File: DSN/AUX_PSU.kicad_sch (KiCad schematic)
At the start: 9 parts

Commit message: Added Footprints
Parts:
- U?: footprint (none) -> Package_TO_SOT_SMD:SOT-563; MFR PN (none) -> TPS62A02ADRLR
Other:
- title: (none) -> 3V3 Aux PSU
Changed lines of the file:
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@@
 (kicad_sch (version 20211123) (generator eeschema)
   (paper "A4")
+  (title_block
+    (title "3V3 Aux PSU")
+    (date "2023-03-07")
+    (rev "A")
+    (comment 1 "Designed by DragonEnjouer :3")
+  )
   (junction (at 185.42 88.9) (diameter 0) (color 0 0 0 0)
   )
@@
     (property "Reference" "U?" (id 0) (at 128.27 81.28 0))
     (property "Value" "TPS62A02A" (id 1) (at 128.27 83.82 0))
-    (property "Footprint" "" (id 2) (at 144.78 92.71 0)
-      (effects (font (size 1.27 1.27)) hide)
-    )
-    (property "Datasheet" "" (id 3) (at 144.78 92.71 0)
-      (effects (font (size 1.27 1.27)) hide)
-    )
+    (property "Footprint" "Package_TO_SOT_SMD:SOT-563" (id 2) (at 144.78 92.71 0)
+      (effects (font (size 1.27 1.27)) hide)
+    )
+    (property "Datasheet" "https://www.ti.com/lit/ds/symlink/tps62a02a.pdf" (id 3) (at 144.78 92.71 0)
+      (effects (font (size 1.27 1.27)) hide)
+    )
+    (property "MFR PN" "TPS62A02ADRLR" (id 4) (at 119.38 101.6 0)
+      (effects (font (size 1.27 1.27)) hide)
+    )

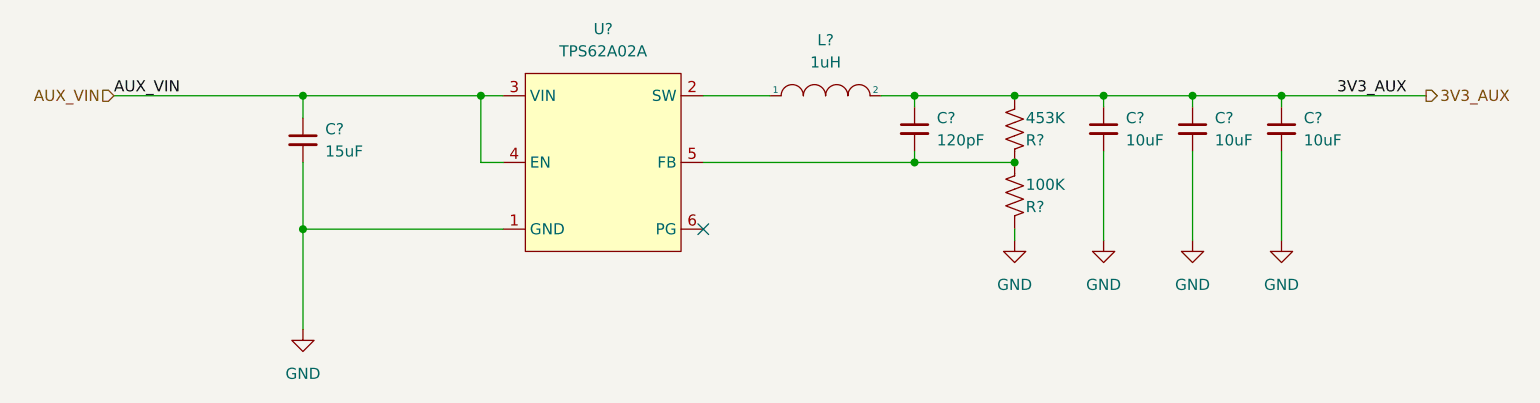
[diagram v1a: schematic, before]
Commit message: Added component ref des
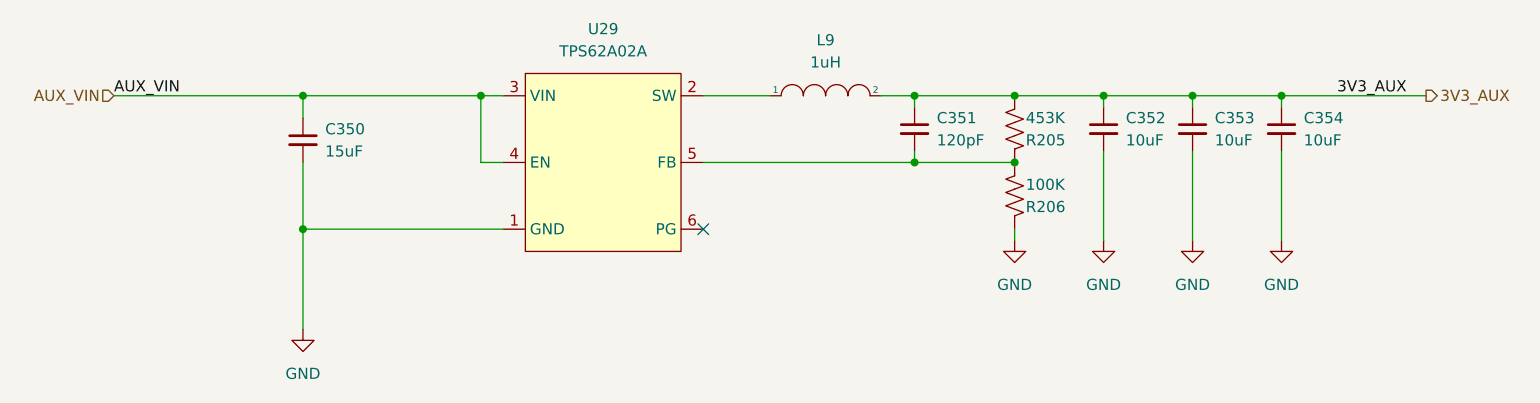
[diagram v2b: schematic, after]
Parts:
- gave numbers to parts that had none: 9
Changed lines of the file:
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@@
   (symbol (lib_id "Device:C_Small") (at 185.42 92.71 0) (unit 1)
     (in_bom yes) (on_board yes) (fields_autoplaced)
-    (property "Reference" "C?" (id 0) (at 187.96 91.4462 0)
+    (property "Reference" "C352" (id 0) (at 187.96 91.4462 0)
       (effects (font (size 1.27 1.27)) (justify left))
     )
@@
   (symbol (lib_id "power:GND") (at 175.26 105.41 0) (unit 1)
     (in_bom yes) (on_board yes) (fields_autoplaced)
-    (property "Reference" "#PWR?" (id 0) (at 175.26 111.76 0)
+    (property "Reference" "#PWR0579" (id 0) (at 175.26 111.76 0)
       (effects (font (size 1.27 1.27)) hide)
     )
@@
   (symbol (lib_id "pspice:INDUCTOR") (at 153.67 88.9 0) (unit 1)
     (in_bom yes) (on_board yes) (fields_autoplaced)
-    (property "Reference" "L?" (id 0) (at 153.67 82.55 0))
+    (property "Reference" "L9" (id 0) (at 153.67 82.55 0))
     (property "Value" "1uH" (id 1) (at 153.67 85.09 0))
     (property "Footprint" "Inductor_SMD:L_1008_2520Metric" (id 2) (at 153.67 88.9 0)
@@
   (symbol (lib_id "power:GND") (at 93.98 115.57 0) (unit 1)
     (in_bom yes) (on_board yes) (fields_autoplaced)
-    (property "Reference" "#PWR?" (id 0) (at 93.98 121.92 0)
+    (property "Reference" "#PWR0578" (id 0) (at 93.98 121.92 0)
       (effects (font (size 1.27 1.27)) hide)
     )
@@
   (symbol (lib_id "Device:C_Small") (at 93.98 93.98 0) (unit 1)
     (in_bom yes) (on_board yes) (fields_autoplaced)
-    (property "Reference" "C?" (id 0) (at 96.52 92.7162 0)
+    (property "Reference" "C350" (id 0) (at 96.52 92.7162 0)
       (effects (font (size 1.27 1.27)) (justify left))
     )
@@
   (symbol (lib_id "Device:C_Small") (at 163.83 92.71 0) (unit 1)
     (in_bom yes) (on_board yes) (fields_autoplaced)
-    (property "Reference" "C?" (id 0) (at 166.37 91.4462 0)
+    (property "Reference" "C351" (id 0) (at 166.37 91.4462 0)
       (effects (font (size 1.27 1.27)) (justify left))
     )
@@
   (symbol (lib_id "Device:C_Small") (at 195.58 92.71 0) (unit 1)
     (in_bom yes) (on_board yes) (fields_autoplaced)
-    (property "Reference" "C?" (id 0) (at 198.12 91.4462 0)
+    (property "Reference" "C353" (id 0) (at 198.12 91.4462 0)
       (effects (font (size 1.27 1.27)) (justify left))
     )
@@
   (symbol (lib_id "Device:C_Small") (at 205.74 92.71 0) (unit 1)
     (in_bom yes) (on_board yes) (fields_autoplaced)
-    (property "Reference" "C?" (id 0) (at 208.28 91.4462 0)
+    (property "Reference" "C354" (id 0) (at 208.28 91.4462 0)
       (effects (font (size 1.27 1.27)) (justify left))
     )
@@
   (symbol (lib_id "Device:R_US") (at 175.26 92.71 0) (mirror y) (unit 1)
     (in_bom yes) (on_board yes)
-    (property "Reference" "R?" (id 0) (at 176.53 93.98 0)
+    (property "Reference" "R205" (id 0) (at 176.53 93.98 0)
       (effects (font (size 1.27 1.27)) (justify right))
     )
@@
   (symbol (lib_id "power:GND") (at 205.74 105.41 0) (unit 1)
     (in_bom yes) (on_board yes) (fields_autoplaced)
-    (property "Reference" "#PWR?" (id 0) (at 205.74 111.76 0)
+    (property "Reference" "#PWR0582" (id 0) (at 205.74 111.76 0)
       (effects (font (size 1.27 1.27)) hide)
     )
@@
   (symbol (lib_id "Device:R_US") (at 175.26 100.33 0) (mirror y) (unit 1)
     (in_bom yes) (on_board yes)
-    (property "Reference" "R?" (id 0) (at 176.53 101.6 0)
+    (property "Reference" "R206" (id 0) (at 176.53 101.6 0)
       (effects (font (size 1.27 1.27)) (justify right))
     )
@@
   (symbol (lib_id "Regulator_Switching:TPS62A02A") (at 119.38 101.6 0) (unit 1)
     (in_bom yes) (on_board yes) (fields_autoplaced)
-    (property "Reference" "U?" (id 0) (at 128.27 81.28 0))
+    (property "Reference" "U29" (id 0) (at 128.27 81.28 0))
     (property "Value" "TPS62A02A" (id 1) (at 128.27 83.82 0))
     (property "Footprint" "Package_TO_SOT_SMD:SOT-563" (id 2) (at 144.78 92.71 0)
@@
   (symbol (lib_id "power:GND") (at 185.42 105.41 0) (unit 1)
     (in_bom yes) (on_board yes) (fields_autoplaced)
-    (property "Reference" "#PWR?" (id 0) (at 185.42 111.76 0)
+    (property "Reference" "#PWR0580" (id 0) (at 185.42 111.76 0)
       (effects (font (size 1.27 1.27)) hide)
     )
@@
   (symbol (lib_id "power:GND") (at 195.58 105.41 0) (unit 1)
     (in_bom yes) (on_board yes) (fields_autoplaced)
-    (property "Reference" "#PWR?" (id 0) (at 195.58 111.76 0)
-      (effects (font (size 1.27 1.27)) hide)
-    )
+    (property "Reference" "#PWR0581" (id 0) (at 195.58 111.76 0)
+      (effects (font (size 1.27 1.27)) hide)
+    )

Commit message: Fixed all ERC Errors
Warnings can be ignored
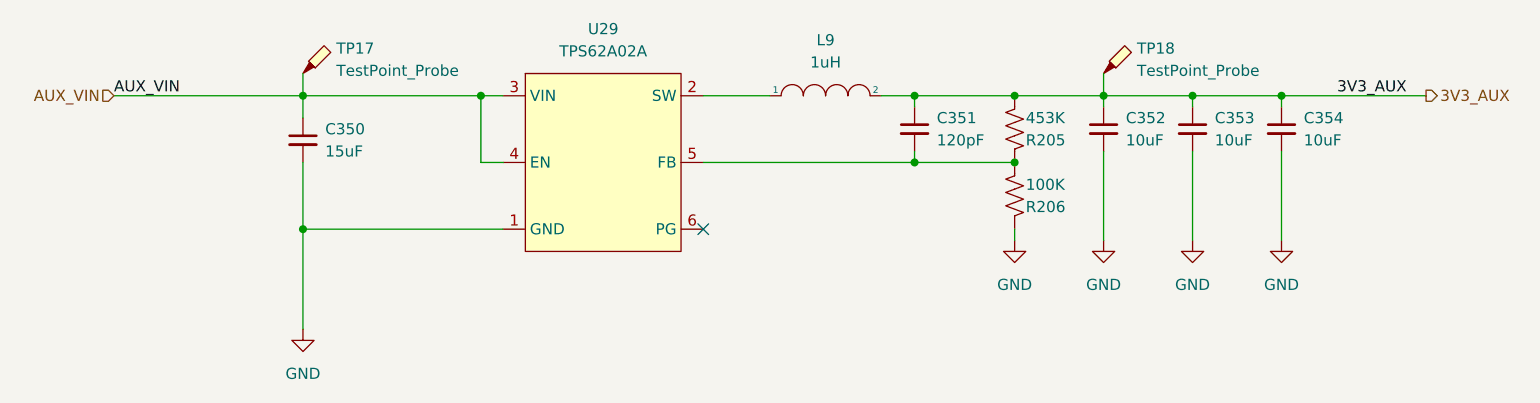
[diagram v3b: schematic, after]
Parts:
- added TP17, TP18: TestPoint_Probe, TestPoint:TestPoint_Loop_D2.50mm_Drill1.85mm, symbol Connector:TestPoint_Probe
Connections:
- net 3V3_AUX: now also TP18.1
- net AUX_VIN: now also TP17.1
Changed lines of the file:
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@@
+    (stroke (width 0) (type default) (color 0 0 0 0))
+  )
+  (wire (pts (xy 93.98 86.36) (xy 93.98 88.9))
     (stroke (width 0) (type default) (color 0 0 0 0))
   )
@@
   )
   (wire (pts (xy 185.42 95.25) (xy 185.42 105.41))
+    (stroke (width 0) (type default) (color 0 0 0 0))
+  )
+  (wire (pts (xy 185.42 86.36) (xy 185.42 88.9))
     (stroke (width 0) (type default) (color 0 0 0 0))
   )
@@
     (pin "1")
     (pin "2")
+  )
+  (symbol (lib_id "Connector:TestPoint_Probe") (at 185.42 86.36 0) (unit 1)
+    (in_bom yes) (on_board yes)
+    (property "Reference" "TP18" (id 0) (at 189.23 83.5024 0)
+      (effects (font (size 1.27 1.27)) (justify left))
+    )
+    (property "Value" "TestPoint_Probe" (id 1) (at 189.23 86.0424 0)
+      (effects (font (size 1.27 1.27)) (justify left))
+    )
+    (property "Footprint" "TestPoint:TestPoint_Loop_D2.50mm_Drill1.85mm" (id 2) (at 190.5 86.36 0)
+      (effects (font (size 1.27 1.27)) hide)
+    )
+    (property "Datasheet" "~" (id 3) (at 190.5 86.36 0)
+      (effects (font (size 1.27 1.27)) hide)
+    )
+    (pin "1")
   )
   (symbol (lib_id "power:GND") (at 93.98 115.57 0) (unit 1)
@@
       (effects (font (size 1.27 1.27)) hide)
     )
+    (pin "1")
+  )
+  (symbol (lib_id "Connector:TestPoint_Probe") (at 93.98 86.36 0) (unit 1)
+    (in_bom yes) (on_board yes)
+    (property "Reference" "TP17" (id 0) (at 97.79 83.5024 0)
+      (effects (font (size 1.27 1.27)) (justify left))
+    )
+    (property "Value" "TestPoint_Probe" (id 1) (at 97.79 86.0424 0)
+      (effects (font (size 1.27 1.27)) (justify left))
+    )
+    (property "Footprint" "TestPoint:TestPoint_Loop_D2.50mm_Drill1.85mm" (id 2) (at 99.06 86.36 0)
+      (effects (font (size 1.27 1.27)) hide)
+    )
+    (property "Datasheet" "~" (id 3) (at 99.06 86.36 0)
+      (effects (font (size 1.27 1.27)) hide)
+    )

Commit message: Updated Layout
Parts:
- removed TP17: TestPoint_Probe, TestPoint:TestPoint_Loop_D2.50mm_Drill1.85mm, symbol Connector:TestPoint_Probe
- added TP21: TestPoint_Probe, TestPoint:TestPoint_Loop_D1.80mm_Drill1.0mm_Beaded, symbol Connector:TestPoint_Probe
- TP18: footprint TestPoint:TestPoint_Loop_D2.50mm_Drill1.85mm -> TestPoint:TestPoint_Loop_D1.80mm_Drill1.0mm_Beaded
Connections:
- net 3V3_AUX: now also TP21.1; no longer TP18.1
- net AUX_VIN: now also TP18.1
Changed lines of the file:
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@@
     (pin "2")
   )
-  (symbol (lib_id "Connector:TestPoint_Probe") (at 185.42 86.36 0) (unit 1)
-    (in_bom yes) (on_board yes)
-    (property "Reference" "TP18" (id 0) (at 189.23 83.5024 0)
-      (effects (font (size 1.27 1.27)) (justify left))
-    )
-    (property "Value" "TestPoint_Probe" (id 1) (at 189.23 86.0424 0)
-      (effects (font (size 1.27 1.27)) (justify left))
-    )
-    (property "Footprint" "TestPoint:TestPoint_Loop_D2.50mm_Drill1.85mm" (id 2) (at 190.5 86.36 0)
-      (effects (font (size 1.27 1.27)) hide)
-    )
-    (property "Datasheet" "~" (id 3) (at 190.5 86.36 0)
+  (symbol (lib_id "Connector:TestPoint_Probe") (at 93.98 86.36 0) (unit 1)
+    (in_bom yes) (on_board yes)
+    (property "Reference" "TP18" (id 0) (at 97.79 83.5024 0)
+      (effects (font (size 1.27 1.27)) (justify left))
+    )
+    (property "Value" "TestPoint_Probe" (id 1) (at 97.79 86.0424 0)
+      (effects (font (size 1.27 1.27)) (justify left))
+    )
+    (property "Footprint" "TestPoint:TestPoint_Loop_D1.80mm_Drill1.0mm_Beaded" (id 2) (at 99.06 86.36 0)
+      (effects (font (size 1.27 1.27)) hide)
+    )
+    (property "Datasheet" "~" (id 3) (at 99.06 86.36 0)
       (effects (font (size 1.27 1.27)) hide)
     )
@@
     (pin "1")
     (pin "2")
+  )
+  (symbol (lib_id "Connector:TestPoint_Probe") (at 185.42 86.36 0) (unit 1)
+    (in_bom yes) (on_board yes)
+    (property "Reference" "TP21" (id 0) (at 189.23 83.5024 0)
+      (effects (font (size 1.27 1.27)) (justify left))
+    )
+    (property "Value" "TestPoint_Probe" (id 1) (at 189.23 86.0424 0)
+      (effects (font (size 1.27 1.27)) (justify left))
+    )
+    (property "Footprint" "TestPoint:TestPoint_Loop_D1.80mm_Drill1.0mm_Beaded" (id 2) (at 190.5 86.36 0)
+      (effects (font (size 1.27 1.27)) hide)
+    )
+    (property "Datasheet" "~" (id 3) (at 190.5 86.36 0)
+      (effects (font (size 1.27 1.27)) hide)
+    )
+    (pin "1")
   )
   (symbol (lib_id "power:GND") (at 205.74 105.41 0) (unit 1)
@@
       (effects (font (size 1.27 1.27)) hide)
     )
-    (pin "1")
-  )
-  (symbol (lib_id "Connector:TestPoint_Probe") (at 93.98 86.36 0) (unit 1)
-    (in_bom yes) (on_board yes)
-    (property "Reference" "TP17" (id 0) (at 97.79 83.5024 0)
-      (effects (font (size 1.27 1.27)) (justify left))
-    )
-    (property "Value" "TestPoint_Probe" (id 1) (at 97.79 86.0424 0)
-      (effects (font (size 1.27 1.27)) (justify left))
-    )
-    (property "Footprint" "TestPoint:TestPoint_Loop_D2.50mm_Drill1.85mm" (id 2) (at 99.06 86.36 0)
-      (effects (font (size 1.27 1.27)) hide)
-    )
-    (property "Datasheet" "~" (id 3) (at 99.06 86.36 0)
-      (effects (font (size 1.27 1.27)) hide)
-    )
